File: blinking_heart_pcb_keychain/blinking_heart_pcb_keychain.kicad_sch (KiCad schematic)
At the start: 1 part

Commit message: Making more changes
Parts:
- U1: footprint (none) -> blinking_heart_pcb_keychain_footprints:NE555P
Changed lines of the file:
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@@
 			)
 		)
-		(property "Footprint" ""
+		(property "Footprint" "blinking_heart_pcb_keychain_footprints:NE555P"
 			(at 139.7 87.63 0)
 			(hide yes)

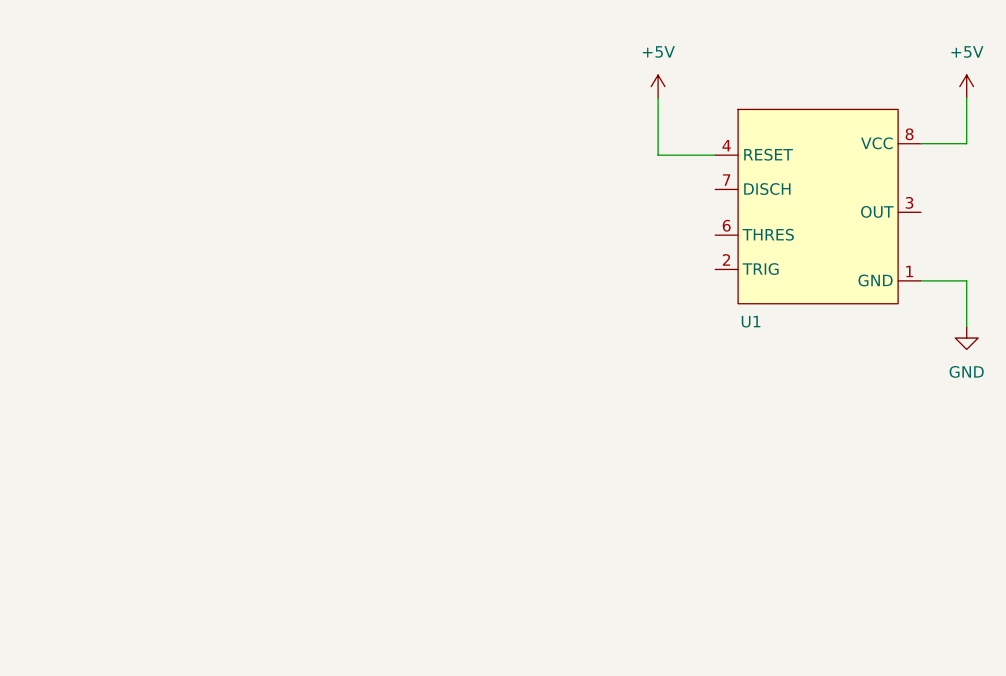
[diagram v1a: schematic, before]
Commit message: Making clock generator circuit
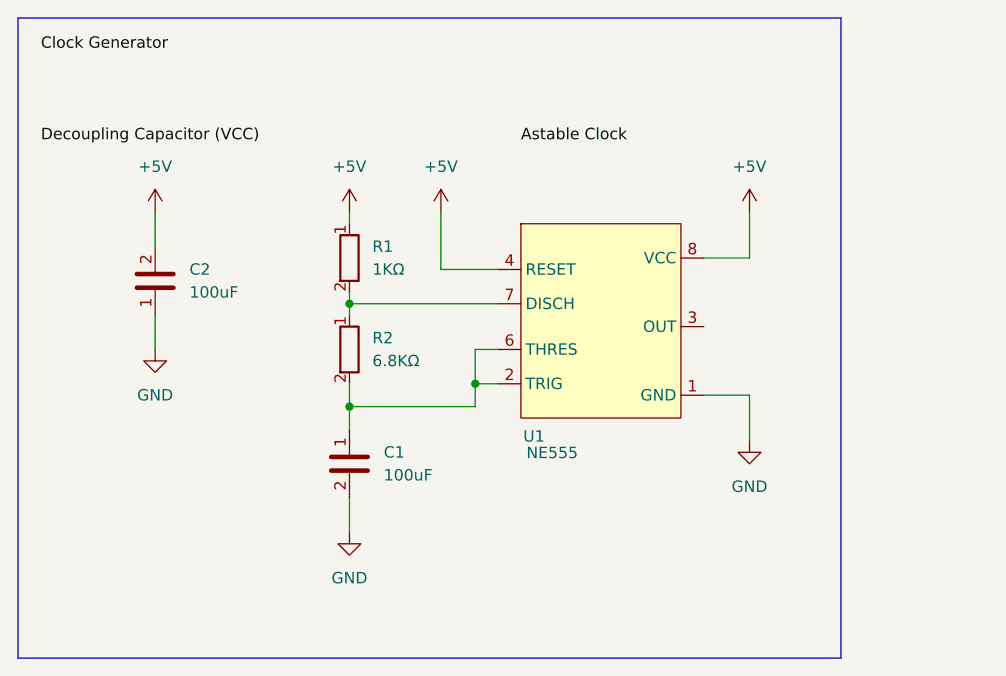
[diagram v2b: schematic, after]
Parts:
- added C1: 100uF, blinking_heart_pcb_keychain_footprints:C_THT_100uF, symbol blinking_heart_pcb_keychain_components:C_THT_100uF
- added C2: 100uF, blinking_heart_pcb_keychain_footprints:C_THT_10nF, symbol blinking_heart_pcb_keychain_components:C_THT_10nF
- added R1: 1KΩ, blinking_heart_pcb_keychain_footprints:R THT 1KΩ, symbol blinking_heart_pcb_keychain_components:Resistor_THT_1KΩ
- added R2: 6.8KΩ, blinking_heart_pcb_keychain_footprints:R THT 1KΩ, symbol blinking_heart_pcb_keychain_components:Resistor_THT_6.8KΩ
- U1: value (none) -> NE555
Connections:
- net +5V: now also C2.2, R1.1
- net GND: now also C1.2, C2.1
- net at U1.2 (TRIG): now also U1.6 (THRES), C1.1, R2.2
- net at U1.7 (DISCH): now also R1.2, R2.1
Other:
- moved on the sheet: U1

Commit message: Building counter circuit
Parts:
- added D1, D10, D2, D3, D4, D5, D6, D7, D8, D9: (no value), blinking_heart_pcb_keychain_footprints:LED_THT_RED, symbol blinking_heart_pcb_keychain_components:LED_Red
- added R10, R11, R12, R3, R4, R5, R6, R7, R8, R9: 130Ω, blinking_heart_pcb_keychain_footprints:R_THT_130Ω, symbol blinking_heart_pcb_keychain_components:R_THT_130Ω
- added U2: CD4017BE, blinking_heart_pcb_keychain_footprints:CD4017BE, symbol blinking_heart_pcb_keychain_components:CD4017B
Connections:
- net +5V: now also U2.16 (+5V)
- net GND: now also R10.2, R11.2, R12.2, R3.2, R4.2, R5.2, R6.2, R7.2, R8.2, R9.2, U2.13 (CLK_PAUSE), U2.15 (RESET), U2.8 (GND)
- net CLK: now reaches U1.3 (OUT)
- net CLK: now also U2.14 (CLK)
- new net: D8.1, R10.1
- new net: D8.2, U2.6 (OUT_7)
- new net: D10.1, R12.1
- new net: D10.2, U2.11 (OUT_9)
- new net: D9.1, R11.1
- new net: D9.2, U2.9 (OUT_8)
- new net: D1.1, R3.1
- new net: D7.1, R9.1
- new net: D7.2, U2.5 (OUT_6)
- new net: D6.1, R8.1
- new net: D6.2, U2.1 (OUT_5)
- new net: D1.2, U2.3 (OUT_0)
- new net: D2.1, R4.1
- new net: D2.2, U2.2 (OUT_1)
- new net: D5.2, U2.10 (OUT_4)
- new net: D3.2, U2.4 (OUT_2)
- new net: D4.2, U2.7 (OUT_3)
- new net: D3.1, R5.1
- new net: D5.1, R7.1
- new net: D4.1, R6.1
- no-connect marks 0 -> 1
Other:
- note added: "Astable Clock"
- note added: "Clock Generator"
- note added: "Counter & LEDs"
- note added: "Decoupling Capacitor (VCC)"
- moved on the sheet: C1, C2, R1, R2, U1

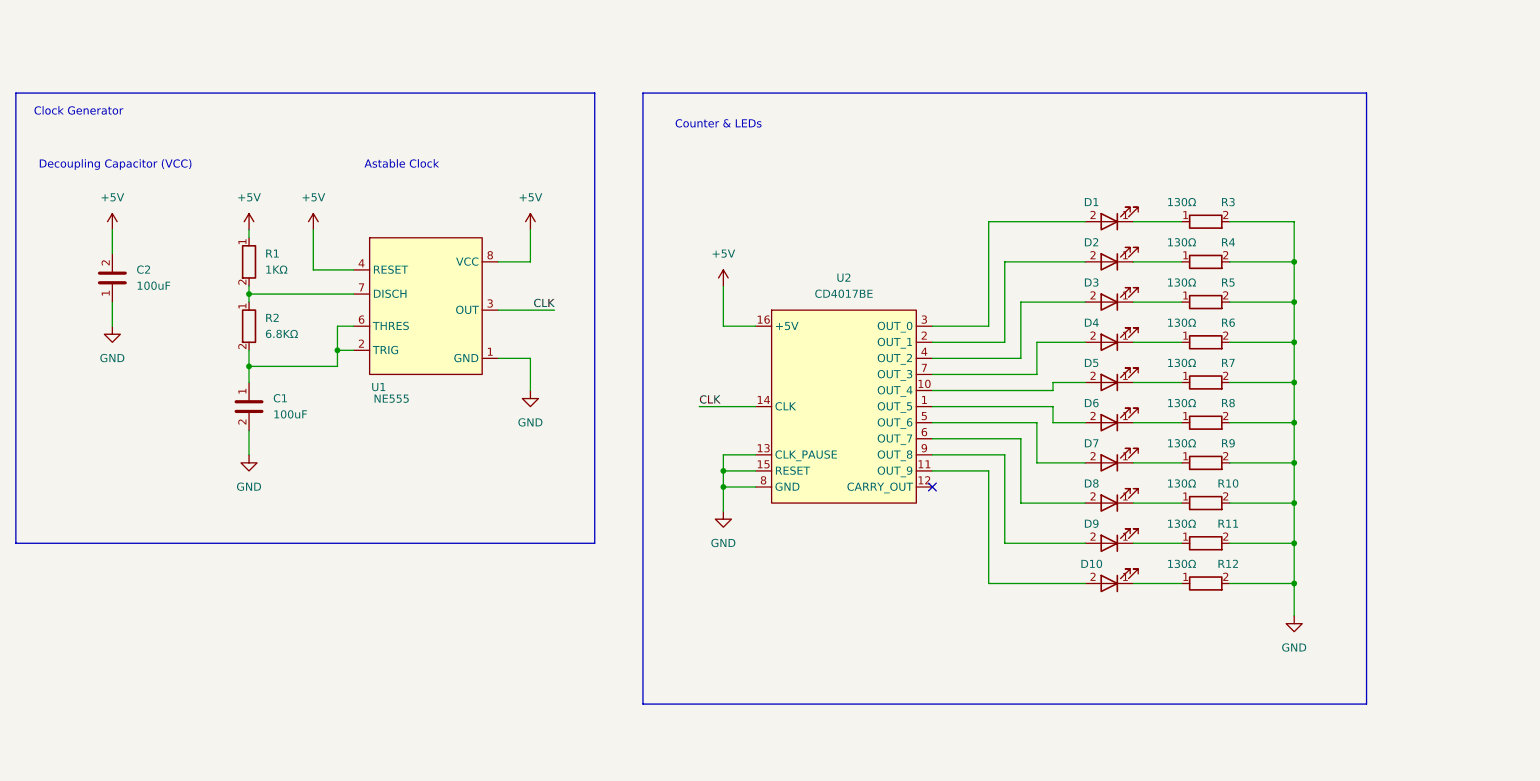
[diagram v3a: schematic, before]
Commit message: Adding power circuit to the schematic
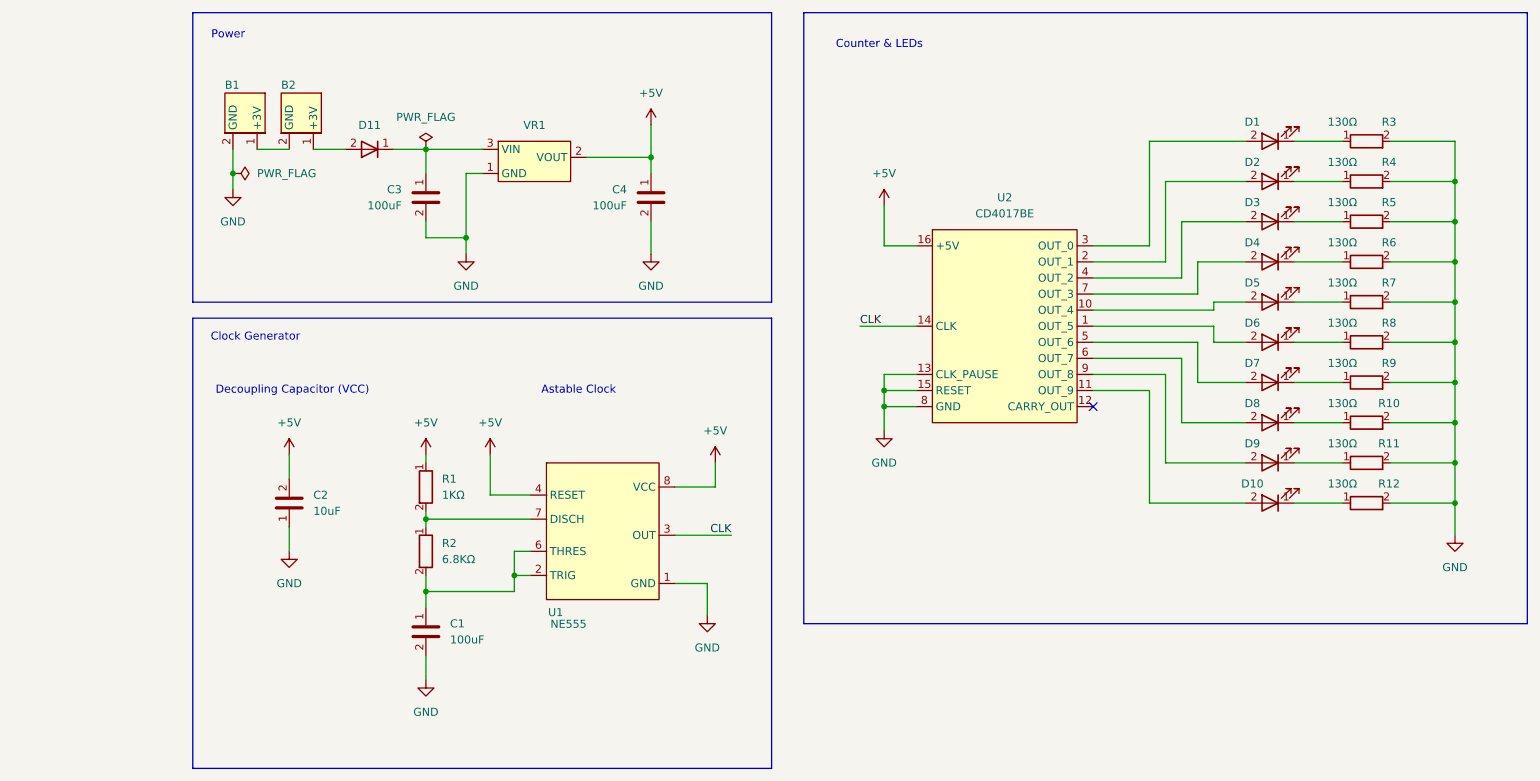
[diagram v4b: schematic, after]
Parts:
- added B1, B2: +3V, blinking_heart_pcb_keychain_footprints:B_CR2032, symbol blinking_heart_pcb_keychain_components:B_CR2032
- added C3, C4: 100uF, blinking_heart_pcb_keychain_footprints:C_THT_100uF, symbol blinking_heart_pcb_keychain_components:C_THT_100uF
- added D11: (no value), blinking_heart_pcb_keychain_footprints:D_1N5817, symbol blinking_heart_pcb_keychain_components:D
- added VR1: 5V, blinking_heart_pcb_keychain_footprints:VR_5V, symbol blinking_heart_pcb_keychain_components:VR_5V
- C2: value 100uF -> 10uF
- U1: Digikey (none) -> https://www.digikey.ca/short/58z8bnmq
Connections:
- net +5V: now also C4.1, VR1.2 (VOUT)
- net GND: now also B1.2 (GND), C3.2, C4.2, VR1.1 (GND)
- new net: C3.1, D11.1, VR1.3 (VIN)
- new net: B2.1 (+3V), D11.2
- new net: B1.1 (+3V), B2.2 (GND)
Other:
- note added: "Power"
- moved on the sheet: C1, C2, D1, D10, D2, D3, D4, D5, D6, D7, D8, D9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
